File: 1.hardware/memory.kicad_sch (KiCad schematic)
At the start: 71 parts, among them IC3 IS42S32800J-6TLI, U5 W25Q128JVS, U6 NC_IS42S16400J-xC

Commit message: 풋프린트 연결 완료
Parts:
- IC3: footprint SamacSys_Parts:SOP50P1176X120-86N -> SamacSys_Parts_Project:SOP50P1176X120-86N
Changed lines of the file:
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@@
 			)
 		)
-		(property "Footprint" "SamacSys_Parts:SOP50P1176X120-86N"
+		(property "Footprint" "SamacSys_Parts_Project:SOP50P1176X120-86N"
 			(at 384.81 77.47 0)
 			(effects

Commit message: 중간 저장
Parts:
- renumbered C62 to C64, C63 to C65, C64 to C66, C65 to C67, C66 to C68, C67 to C69, C68 to C70, C69 to C71, C70 to C72, C71 to C73, C72 to C74, C73 to C75, IC3 to IC2, R50 to R38, R51 to R39, R52 to R40, R53 to R41, R54 to R42, R55 to R43, R56 to R44, R57 to R45, R58 to R46, R59 to R47, R60 to R48, R61 to R49, R62 to R50, R63 to R51, R64 to R52, R65 to R53, R66 to R54, R67 to R55, R68 to R56, R69 to R57, R70 to R58, R71 to R59, R72 to R60, R73 to R61, R74 to R62, R75 to R63, R76 to R64, R77 to R65, R78 to R66, R79 to R67, R80 to R68, R81 to R69, R82 to R70, R83 to R71, R84 to R72, R85 to R73, R86 to R74, R87 to R75, R88 to R76, R89 to R77, R90 to R78, R91 to R79, R92 to R80, R93 to R81, R94 to R82, R95 to R83, R96 to R84, R97 to R85, R98 to R86, R99 to R87, R100 to R88, R101 to R89, R102 to R90, R103 to R91, R104 to R92, R105 to R93, U5 to U6, U6 to U7

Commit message: 중간 저장
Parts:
- added C68, C69, C70, C71: 0.1uF/50V, Capacitor_SMD:C_0603_1608Metric, symbol Device:C_Small_US
- added U11, U12, U13, U14, U15, U16, U18, U19, U20, U21, U6, U7, U8, U9: 4D02WGJ0330T, 4D02_2X1_ROH, symbol 2025-12-16_06-00-56:4D02WGJ0330T
- R34: renamed from R38; now not fitted; now left out of the parts list
- R35: renamed from R62; now not fitted; now left out of the parts list
- R36: renamed from R39; now not fitted; now left out of the parts list
- R37: renamed from R63; now not fitted; now left out of the parts list
- R38: renamed from R40; now not fitted; now left out of the parts list
- R39: renamed from R64; now not fitted; now left out of the parts list
- R40: renamed from R41; now not fitted; now left out of the parts list
- R41: renamed from R65; now not fitted; now left out of the parts list
- R42: now not fitted; now left out of the parts list
- R43: renamed from R66; now not fitted; now left out of the parts list
- R44: renamed from R43; now not fitted; now left out of the parts list
- R45: renamed from R67; now not fitted; now left out of the parts list
- R46: renamed from R44; now not fitted; now left out of the parts list
- R47: renamed from R68; now not fitted; now left out of the parts list
- R48: renamed from R45; now not fitted; now left out of the parts list
- R49: renamed from R69; now not fitted; now left out of the parts list
- R50: renamed from R46; now not fitted; now left out of the parts list
- R51: renamed from R70; now not fitted; now left out of the parts list
- R52: renamed from R47; now not fitted; now left out of the parts list
- R53: renamed from R71; now not fitted; now left out of the parts list
- R54: renamed from R48; now not fitted; now left out of the parts list
- R55: renamed from R72; now not fitted; now left out of the parts list
- R56: renamed from R49; now not fitted; now left out of the parts list
- R57: renamed from R73; now not fitted; now left out of the parts list
- R58: renamed from R74; now not fitted; now left out of the parts list
- R59: renamed from R50; now not fitted; now left out of the parts list
- R60: renamed from R75; now not fitted; now left out of the parts list
- R61: renamed from R51; now not fitted; now left out of the parts list
- R62: renamed from R76; now not fitted; now left out of the parts list
- R63: renamed from R77; now not fitted; now left out of the parts list
- R64: renamed from R52; now not fitted; now left out of the parts list
- R65: renamed from R78; now not fitted; now left out of the parts list
- R66: renamed from R53; now not fitted; now left out of the parts list
- R67: renamed from R79; now not fitted; now left out of the parts list
- R68: renamed from R54; now not fitted; now left out of the parts list
- R69: renamed from R80; now not fitted; now left out of the parts list
- R70: renamed from R55; now not fitted; now left out of the parts list
- R71: renamed from R81; now not fitted; now left out of the parts list
- R72: renamed from R56; now not fitted; now left out of the parts list
- R73: renamed from R82; now not fitted; now left out of the parts list
- R74: renamed from R57; now not fitted; now left out of the parts list
- R75: renamed from R83; now not fitted; now left out of the parts list
- R76: renamed from R84; now not fitted; now left out of the parts list
- R77: renamed from R85; now not fitted; now left out of the parts list
- R78: renamed from R58; now not fitted; now left out of the parts list
- R79: renamed from R86; now not fitted; now left out of the parts list
- R80: renamed from R59; now not fitted; now left out of the parts list
- R81: renamed from R87; now not fitted; now left out of the parts list
- R82: renamed from R60; now not fitted; now left out of the parts list
- R83: renamed from R88; now not fitted; now left out of the parts list
- R84: renamed from R61; now not fitted; now left out of the parts list
- R85: renamed from R89; now not fitted; now left out of the parts list
- R86: renamed from R90; now not fitted; now left out of the parts list
- R87: renamed from R91; now not fitted; now left out of the parts list
- R88: renamed from R92; now not fitted; now left out of the parts list
- R89: renamed from R93; now not fitted; now left out of the parts list
- renumbered C68 to C60, C70 to C61, C72 to C62, C74 to C63, C69 to C64, C71 to C65, C73 to C66, C75 to C67, C64 to C72, C65 to C73, C66 to C74, C67 to C75, IC2 to IC3, U6 to U10, U7 to U17
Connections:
- net 3V3_MCU: now also C68.1, C69.1, C70.1, C71.1
- net FMC_A0: now also U15.2
- net FMC_A1: now also U15.3
- net FMC_A10: now also U15.1
- net FMC_A11: now also U13.2
- net FMC_A2: now also U15.4
- net FMC_A3: now also U16.2
- net FMC_A4: now also U16.1
- net FMC_A5: now also U14.4
- net FMC_A6: now also U14.3
- net FMC_A7: now also U14.2
- net FMC_A8: now also U14.1
- net FMC_A9: now also U12.4
- net FMC_BA0: now also U13.3
- net FMC_BA1: now also U13.4
- net FMC_D0: now also U7.1
- net FMC_D1: now also U7.2
- net FMC_D10: now also U8.2
- net FMC_D11: now also U8.1
- net FMC_D12: now also U6.4
- net FMC_D13: now also U6.3
- net FMC_D14: now also U6.2
- net FMC_D15: now also U6.1
- net FMC_D16: now also U18.2
- net FMC_D17: now also U18.3
- net FMC_D18: now also U18.4
- net FMC_D19: now also U20.1
- net FMC_D2: now also U7.3
- net FMC_D20: now also U20.2
- net FMC_D21: now also U20.3
- net FMC_D22: now also U20.4
- net FMC_D23: now also U21.1
- net FMC_D24: now also U21.2
- net FMC_D25: now also U21.3
- net FMC_D26: now also U21.4
- net FMC_D27: now also U19.4
- net FMC_D28: now also U19.3
- net FMC_D29: now also U19.2
- net FMC_D3: now also U7.4
- net FMC_D30: now also U19.1
- net FMC_D31: now also U16.4
- net FMC_D4: now also U9.1
- net FMC_D5: now also U9.2
- net FMC_D6: now also U9.3
- net FMC_D7: now also U9.4
- net FMC_D8: now also U8.4
- net FMC_D9: now also U8.3
- net FMC_NBL0: now also U11.1
- net FMC_NBL1: now also U12.1
- net FMC_NBL2: now also U18.1
- net FMC_NBL3: now also U16.3
- net FMC_SDCKE0: now also U12.3
- net FMC_SDCLK: now also U12.2
- net FMC_SDNCAS: now also U11.3
- net FMC_SDNE0: now also U13.1
- net FMC_SDNRAS: now also U11.4
- net FMC_SDNWE: now also U11.2
- net GND: now also C68.2, C69.2, C70.2, C71.2
- net SDRAM_A0: now also U15.7
- net SDRAM_A1: now also U15.6
- net SDRAM_A10: now also U15.8
- net SDRAM_A11: now also U13.7
- net SDRAM_A2: now also U15.5
- net SDRAM_A3: now also U16.7
- net SDRAM_A4: now also U16.8
- net SDRAM_A5: now also U14.5
- net SDRAM_A6: now also U14.6
- net SDRAM_A7: now also U14.7
- net SDRAM_A8: now also U14.8
- net SDRAM_A9: now also U12.5
- net SDRAM_BA0: now also U13.6
- net SDRAM_BA1: now also U13.5
- net SDRAM_CAS: now also U11.6
- net SDRAM_CKE: now also U12.6
- net SDRAM_CLK: now also U12.7
- net SDRAM_CS: now also U13.8
- net SDRAM_DQ0: now also U7.8
- net SDRAM_DQ1: now also U7.7
- net SDRAM_DQ10: now also U8.7
- net SDRAM_DQ11: now also U8.8
- net SDRAM_DQ12: now also U6.5
- net SDRAM_DQ13: now also U6.6
- net SDRAM_DQ14: now also U6.7
- net SDRAM_DQ15: now also U6.8
- net SDRAM_DQ16: now also U18.7
- net SDRAM_DQ17: now also U18.6
- net SDRAM_DQ18: now also U18.5
- net SDRAM_DQ19: now also U20.8
- net SDRAM_DQ2: now also U7.6
- net SDRAM_DQ20: now also U20.7
- net SDRAM_DQ21: now also U20.6
- net SDRAM_DQ22: now also U20.5
- net SDRAM_DQ23: now also U21.8
- net SDRAM_DQ24: now also U21.7
- net SDRAM_DQ25: now also U21.6
- net SDRAM_DQ26: now also U21.5
- net SDRAM_DQ27: now also U19.5
- net SDRAM_DQ28: now also U19.6
- net SDRAM_DQ29: now also U19.7
- net SDRAM_DQ3: now also U7.5
- net SDRAM_DQ30: now also U19.8
- net SDRAM_DQ31: now also U16.5
- net SDRAM_DQ4: now also U9.8
- net SDRAM_DQ5: now also U9.7
- net SDRAM_DQ6: now also U9.6
- net SDRAM_DQ7: now also U9.5
- net SDRAM_DQ8: now also U8.5
- net SDRAM_DQ9: now also U8.6
- net SDRAM_DQM0: now also U11.8
- net SDRAM_DQM1: now also U12.8
- net SDRAM_DQM2: now also U18.8
- net SDRAM_DQM3: now also U16.6
- net SDRAM_RAS: now also U11.5
- net SDRAM_WE: now also U11.7
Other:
- moved on the sheet: C60, C61, C62, C63, C64, C65, C66, C67, C72, C73, C74, C75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

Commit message: 중간 저장
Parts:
- added C121: 0.1uF/50V, Capacitor_SMD:C_0603_1608Metric, symbol Device:C_Small_US
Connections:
- net 3V3_MCU: now also C121.1
- net FMC_A3: now also U16.3; no longer U16.2
- net FMC_A4: now also U16.4; no longer U16.1
- net FMC_A5: now also U14.1; no longer U14.4
- net FMC_A6: now also U14.2; no longer U14.3
- net FMC_A7: now also U14.3; no longer U14.2
- net FMC_A8: now also U14.4; no longer U14.1
- net FMC_A9: now also U12.1; no longer U12.4
- net FMC_D10: now also U8.3; no longer U8.2
- net FMC_D11: now also U8.4; no longer U8.1
- net FMC_D12: now also U6.1; no longer U6.4
- net FMC_D13: now also U6.2; no longer U6.3
- net FMC_D14: now also U6.3; no longer U6.2
- net FMC_D15: now also U6.4; no longer U6.1
- net FMC_D27: now also U19.1; no longer U19.4
- net FMC_D28: now also U19.2; no longer U19.3
- net FMC_D29: now also U19.3; no longer U19.2
- net FMC_D30: now also U19.4; no longer U19.1
- net FMC_D31: now also U16.1; no longer U16.4
- net FMC_D8: now also U8.1; no longer U8.4
- net FMC_D9: now also U8.2; no longer U8.3
- net FMC_NBL1: now also U12.4; no longer U12.1
- net FMC_NBL3: now also U16.2; no longer U16.3
- net FMC_SDCKE0: now also U12.2; no longer U12.3
- net FMC_SDCLK: now also U12.3; no longer U12.2
- net GND: now also C121.2
- net SDRAM_A3: now also U16.6; no longer U16.7
- net SDRAM_A4: now also U16.5; no longer U16.8
- net SDRAM_A5: now also U14.8; no longer U14.5
- net SDRAM_A6: now also U14.7; no longer U14.6
- net SDRAM_A7: now also U14.6; no longer U14.7
- net SDRAM_A8: now also U14.5; no longer U14.8
- net SDRAM_A9: now also U12.8; no longer U12.5
- net SDRAM_CKE: now also U12.7; no longer U12.6
- net SDRAM_CLK: now also U12.6; no longer U12.7
- net SDRAM_DQ10: now also U8.6; no longer U8.7
- net SDRAM_DQ11: now also U8.5; no longer U8.8
- net SDRAM_DQ12: now also U6.8; no longer U6.5
- net SDRAM_DQ13: now also U6.7; no longer U6.6
- net SDRAM_DQ14: now also U6.6; no longer U6.7
- net SDRAM_DQ15: now also U6.5; no longer U6.8
- net SDRAM_DQ27: now also U19.8; no longer U19.5
- net SDRAM_DQ28: now also U19.7; no longer U19.6
- net SDRAM_DQ29: now also U19.6; no longer U19.7
- net SDRAM_DQ30: now also U19.5; no longer U19.8
- net SDRAM_DQ31: now also U16.8; no longer U16.5
- net SDRAM_DQ8: now also U8.8; no longer U8.5
- net SDRAM_DQ9: now also U8.7; no longer U8.6
- net SDRAM_DQM1: now also U12.5; no longer U12.8
- net SDRAM_DQM3: now also U16.7; no longer U16.6
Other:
- moved on the sheet: C60, C61, C62, C63

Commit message: 오류 일단 다 잡음
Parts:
- C121, C60, C61, C62, C64, C65, C66, C67, C68, C69, C70, C71, C72, C73, C74: footprint Capacitor_SMD:C_0603_1608Metric -> Capacitor_SMD:C_0402_1005Metric
- U11, U12, U13, U14, U15, U16, U18, U19, U20, U21, U6, U7, U8, U9: footprint 4D02_2X1_ROH -> footprints:4D02_2X1_ROH
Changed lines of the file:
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@@
 			)
 		)
-		(property "Footprint" "Capacitor_SMD:C_0603_1608Metric"
+		(property "Footprint" "Capacitor_SMD:C_0402_1005Metric"
 			(at 96.52 48.26 0)
 			(effects
@@
 			)
 		)
-		(property "Footprint" "4D02_2X1_ROH"
+		(property "Footprint" "footprints:4D02_2X1_ROH"
 			(at 173.99 50.8 0)
 			(effects
@@
 			)
 		)
-		(property "Footprint" "4D02_2X1_ROH"
+		(property "Footprint" "footprints:4D02_2X1_ROH"
 			(at 173.99 74.93 0)
 			(effects
@@
 			)
 		)
-		(property "Footprint" "Capacitor_SMD:C_0603_1608Metric"
+		(property "Footprint" "Capacitor_SMD:C_0402_1005Metric"
 			(at 82.55 29.21 0)
 			(effects
@@
 			)
 		)
-		(property "Footprint" "Capacitor_SMD:C_0603_1608Metric"
+		(property "Footprint" "Capacitor_SMD:C_0402_1005Metric"
 			(at 52.07 48.26 0)
 			(effects
@@
 			)
 		)
-		(property "Footprint" "4D02_2X1_ROH"
+		(property "Footprint" "footprints:4D02_2X1_ROH"
 			(at 250.19 49.53 0)
 			(effects
@@
 			)
 		)
-		(property "Footprint" "4D02_2X1_ROH"
+		(property "Footprint" "footprints:4D02_2X1_ROH"
 			(at 250.19 99.06 0)
 			(effects
@@
 			)
 		)
-		(property "Footprint" "4D02_2X1_ROH"
+		(property "Footprint" "footprints:4D02_2X1_ROH"
 			(at 250.19 73.66 0)
 			(effects
@@
 			)
 		)
-		(property "Footprint" "4D02_2X1_ROH"
+		(property "Footprint" "footprints:4D02_2X1_ROH"
 			(at 173.99 171.45 0)
 			(effects
@@
 			)
 		)
-		(property "Footprint" "Capacitor_SMD:C_0603_1608Metric"
+		(property "Footprint" "Capacitor_SMD:C_0402_1005Metric"
 			(at 82.55 48.26 0)
 			(effects
@@
 			)
 		)
-		(property "Footprint" "4D02_2X1_ROH"
+		(property "Footprint" "footprints:4D02_2X1_ROH"
 			(at 251.46 147.32 0)
 			(effects
@@
 			)
 		)
-		(property "Footprint" "Capacitor_SMD:C_0603_1608Metric"
+		(property "Footprint" "Capacitor_SMD:C_0402_1005Metric"
 			(at 127 48.26 0)
 			(effects
@@
 			)
 		)
-		(property "Footprint" "Capacitor_SMD:C_0603_1608Metric"
+		(property "Footprint" "Capacitor_SMD:C_0402_1005Metric"
 			(at 52.07 29.21 0)
 			(effects
@@
 			)
 		)
-		(property "Footprint" "Capacitor_SMD:C_0603_1608Metric"
+		(property "Footprint" "Capacitor_SMD:C_0402_1005Metric"
 			(at 111.76 48.26 0)
 			(effects
@@
 			)
 		)
-		(property "Footprint" "Capacitor_SMD:C_0603_1608Metric"
+		(property "Footprint" "Capacitor_SMD:C_0402_1005Metric"
 			(at 99.06 71.12 0)
 			(effects
@@
 			)
 		)
-		(property "Footprint" "4D02_2X1_ROH"
+		(property "Footprint" "footprints:4D02_2X1_ROH"
 			(at 173.99 147.32 0)
 			(effects
@@
 			)
 		)
-		(property "Footprint" "4D02_2X1_ROH"
+		(property "Footprint" "footprints:4D02_2X1_ROH"
 			(at 227.33 223.52 0)
 			(effects
@@
 			)
 		)
-		(property "Footprint" "Capacitor_SMD:C_0603_1608Metric"
+		(property "Footprint" "Capacitor_SMD:C_0402_1005Metric"
 			(at 113.03 71.12 0)
 			(effects
@@
 			)
 		)
-		(property "Footprint" "Capacitor_SMD:C_0603_1608Metric"
+		(property "Footprint" "Capacitor_SMD:C_0402_1005Metric"
 			(at 67.31 48.26 0)
 			(effects
@@
 			)
 		)
-		(property "Footprint" "Capacitor_SMD:C_0603_1608Metric"
+		(property "Footprint" "Capacitor_SMD:C_0402_1005Metric"
 			(at 36.83 29.21 0)
 			(effects
@@
 			)
 		)
-		(property "Footprint" "Capacitor_SMD:C_0603_1608Metric"
+		(property "Footprint" "Capacitor_SMD:C_0402_1005Metric"
 			(at 142.24 48.26 0)
 			(effects
@@
 			)
 		)
-		(property "Footprint" "4D02_2X1_ROH"
+		(property "Footprint" "footprints:4D02_2X1_ROH"
 			(at 251.46 123.19 0)
 			(effects
@@
 			)
 		)
-		(property "Footprint" "Capacitor_SMD:C_0603_1608Metric"
+		(property "Footprint" "Capacitor_SMD:C_0402_1005Metric"
 			(at 36.83 48.26 0)
 			(effects
@@
 			)
 		)
-		(property "Footprint" "4D02_2X1_ROH"
+		(property "Footprint" "footprints:4D02_2X1_ROH"
 			(at 173.99 195.58 0)
 			(effects
@@
 			)
 		)
-		(property "Footprint" "4D02_2X1_ROH"
+		(property "Footprint" "footprints:4D02_2X1_ROH"
 			(at 251.46 171.45 0)
 			(effects
@@
 			)
 		)
-		(property "Footprint" "Capacitor_SMD:C_0603_1608Metric"
+		(property "Footprint" "Capacitor_SMD:C_0402_1005Metric"
 			(at 85.09 71.12 0)
 			(effects
@@
 			)
 		)
-		(property "Footprint" "Capacitor_SMD:C_0603_1608Metric"
+		(property "Footprint" "Capacitor_SMD:C_0402_1005Metric"
 			(at 67.31 29.21 0)
 			(effects
@@
 			)
 		)
-		(property "Footprint" "4D02_2X1_ROH"
+		(property "Footprint" "footprints:4D02_2X1_ROH"
 			(at 173.99 99.06 0)
 			(effects
@@
 			)
 		)
-		(property "Footprint" "4D02_2X1_ROH"
+		(property "Footprint" "footprints:4D02_2X1_ROH"
 			(at 173.99 123.19 0)
 			(effects

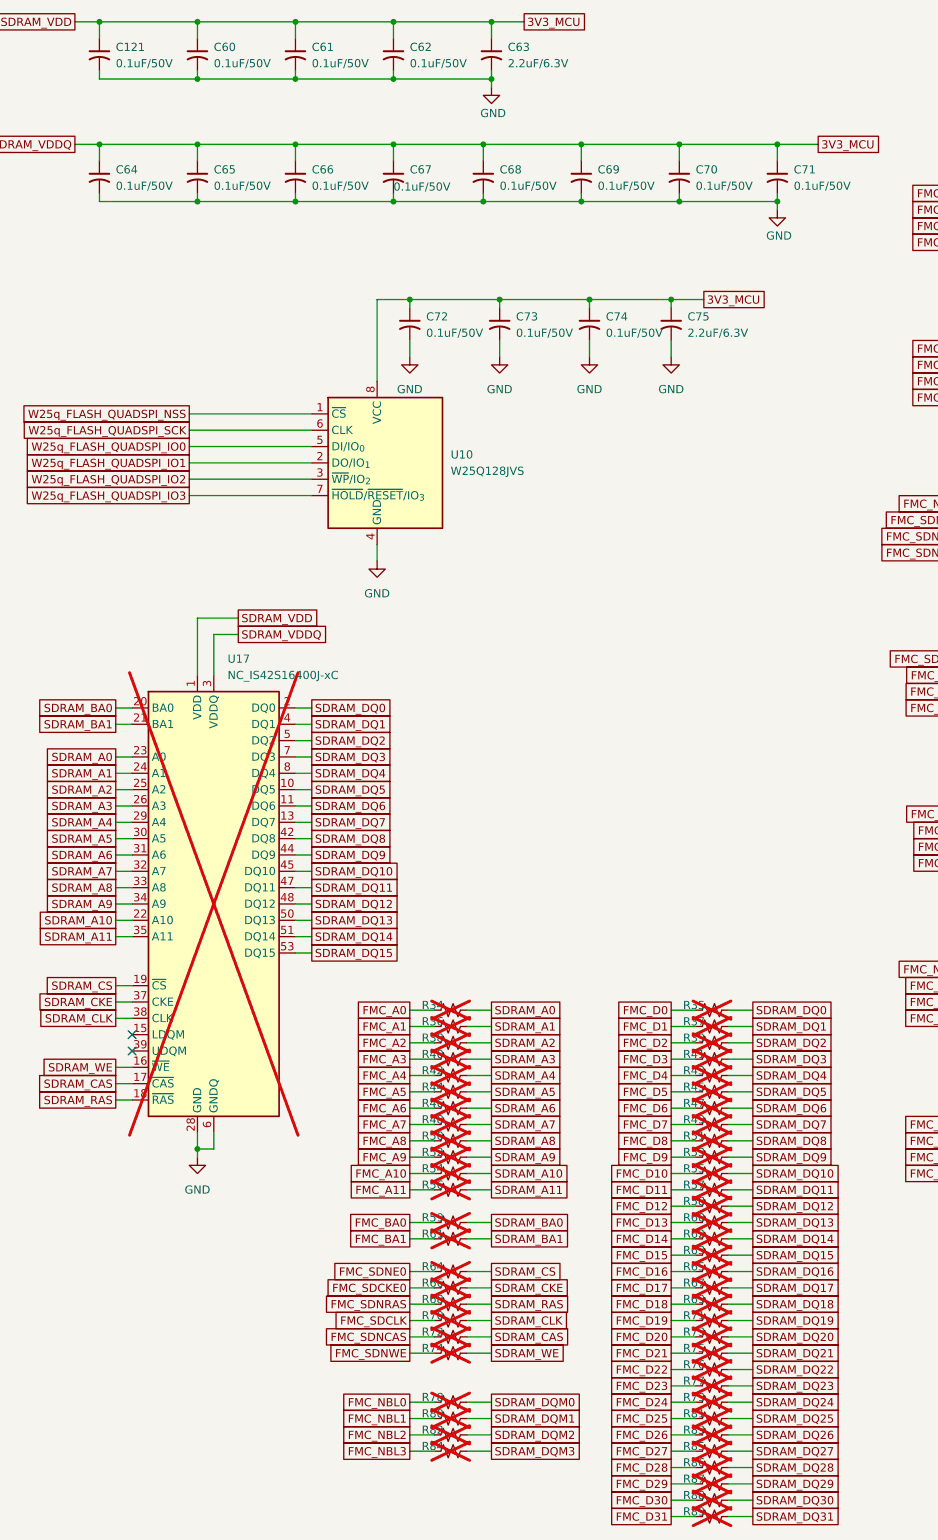
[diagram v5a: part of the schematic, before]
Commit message: 부품 통일 및 필터 부분 캡 선정등 필요해보임
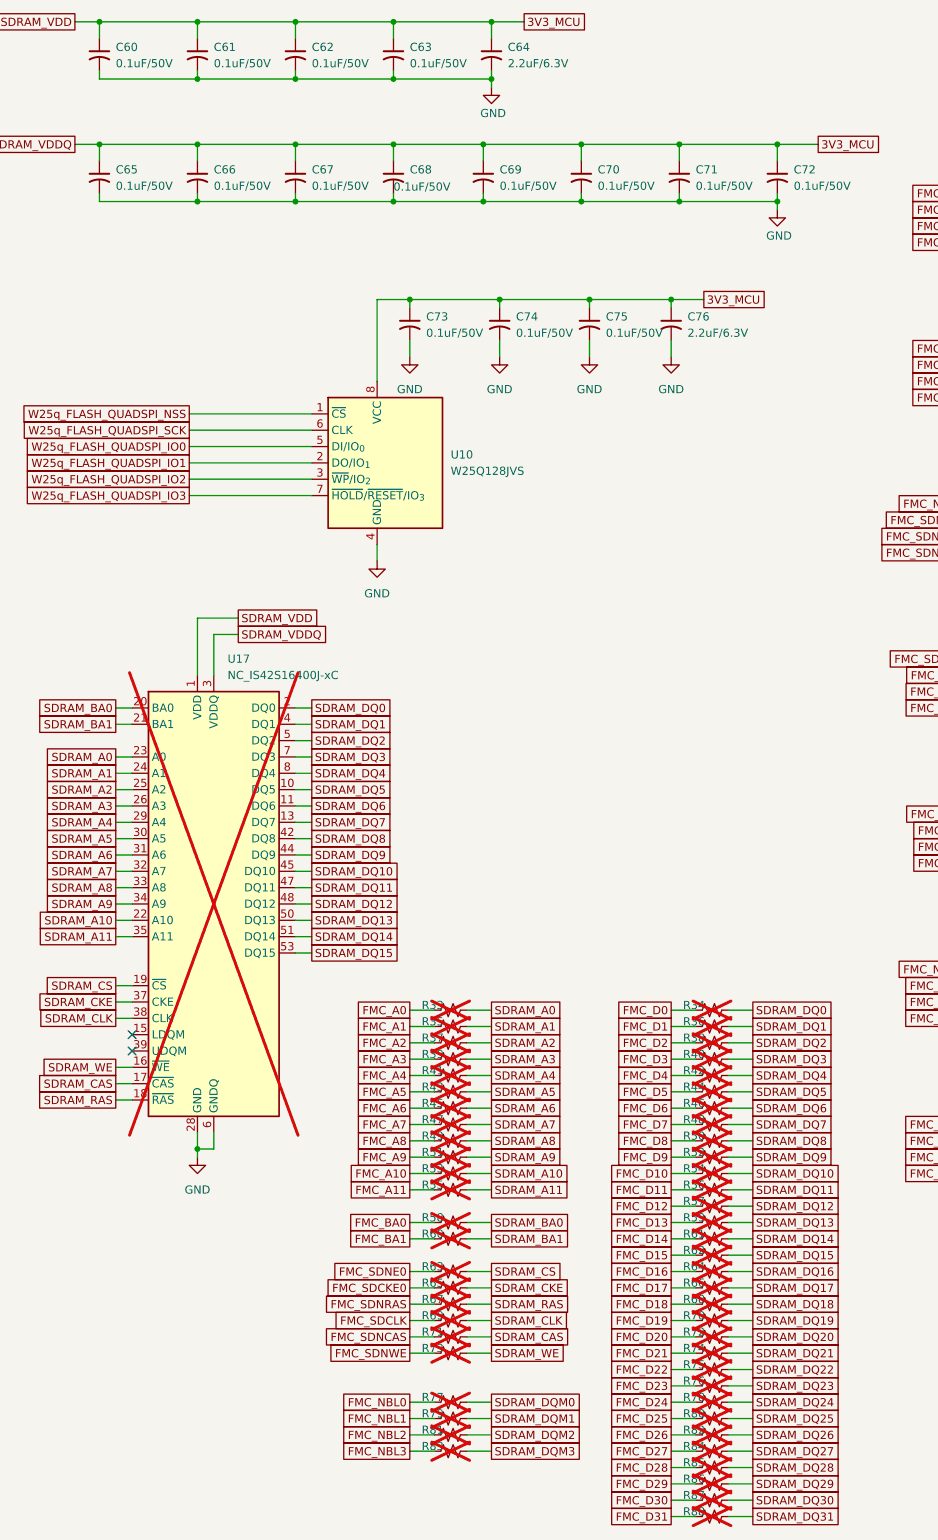
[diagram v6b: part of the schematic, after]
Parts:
- renumbered C121 to C60, C60 to C61, C61 to C62, C62 to C63, C63 to C64, C64 to C65, C65 to C66, C66 to C67, C67 to C68, C68 to C69, C69 to C70, C70 to C71, C71 to C72, C72 to C73, C73 to C74, C74 to C75, C75 to C76, R34 to R33, R35 to R34, R36 to R35, R37 to R36, R38 to R37, R39 to R38, R40 to R39, R41 to R40, R42 to R41, R43 to R42, R44 to R43, R45 to R44, R46 to R45, R47 to R46, R48 to R47, R49 to R48, R50 to R49, R51 to R50, R52 to R51, R53 to R52, R54 to R53, R55 to R54, R56 to R55, R57 to R56, R58 to R57, R59 to R58, R60 to R59, R61 to R60, R62 to R61, R63 to R62, R64 to R63, R65 to R64, R66 to R65, R67 to R66, R68 to R67, R69 to R68, R70 to R69, R71 to R70, R72 to R71, R73 to R72, R74 to R73, R75 to R74, R76 to R75, R77 to R76, R78 to R77, R79 to R78, R80 to R79, R81 to R80, R82 to R81, R83 to R82, R84 to R83, R85 to R84, R86 to R85, R87 to R86, R88 to R87, R89 to R88

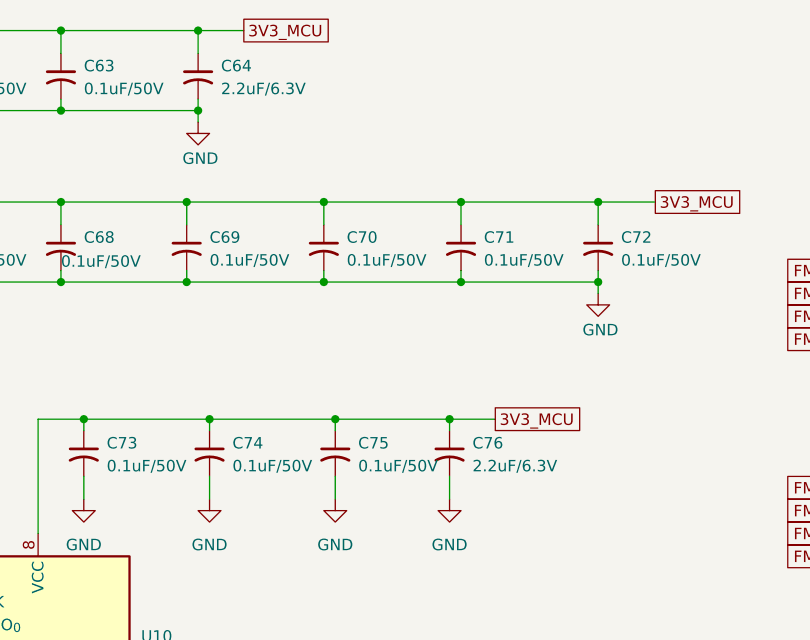
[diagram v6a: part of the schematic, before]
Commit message: 거의 완성 근데 JLC에서 포지션이 좀 개판임
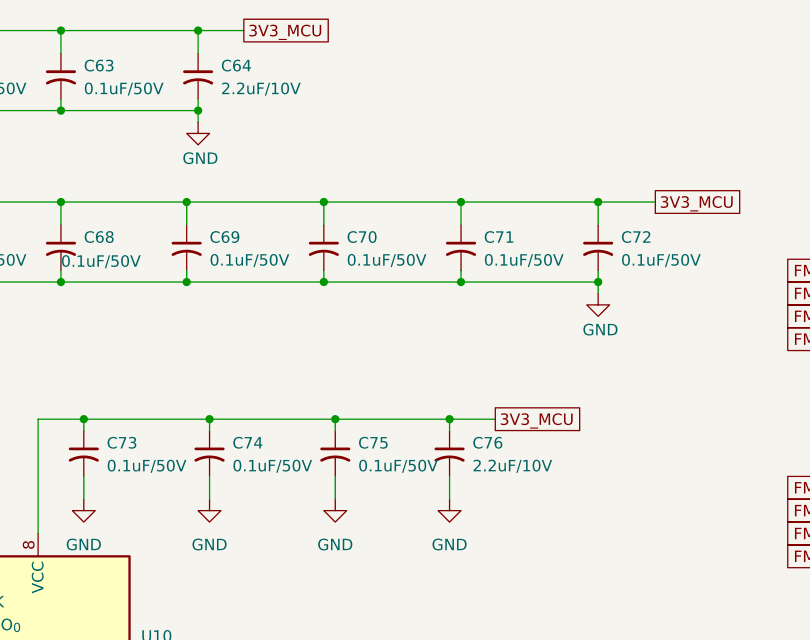
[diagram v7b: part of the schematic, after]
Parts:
- C64, C76: value 2.2uF/6.3V -> 2.2uF/10V
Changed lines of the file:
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@@
 			)
 		)
-		(property "Value" "2.2uF/6.3V"
+		(property "Value" "2.2uF/10V"
 			(at 100.33 30.6069 0)
 			(effects
@@
 			)
 		)
-		(property "Value" "2.2uF/6.3V"
+		(property "Value" "2.2uF/10V"
 			(at 128.27 72.5169 0)
 			(effects
